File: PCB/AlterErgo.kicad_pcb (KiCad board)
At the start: 2 copper layers, 92 parts, among them J1 GS3, J2 SJ-43514, J3 GS3, SW0:10 SW_Push, SW0:11 SW_Push, SW0:12 SW_Push, SW0:7 SW_Push, SW0:8 SW_Push, SW0:9 SW_Push, SW1 SW_SPST, SW1:10 SW_Push, SW1:11 SW_Push, SW1:12 SW_Push, SW1:13 SW_Push, SW1:9 SW_Push, SW2:10 SW_Push, SW2:11 SW_Push, SW2:12 SW_Push, SW2:13 SW_Push, SW2:7 SW_Push, SW2:8 SW_Push, SW2:9 SW_Push, SW3:10 SW_Push, SW3:11 SW_Push, SW3:12 SW_Push, SW3:13 SW_Push, SW3:8 SW_Push, SW3:9 SW_Push, SW4:10 SW_Push, SW4:11 SW_Push, SW4:12 SW_Push, SW4:13 SW_Push, SW4:7 SW_Push, SW4:8 SW_Push, SW4:9 SW_Push, SW5:10 SW_Push, SW5:11 SW_Push, SW5:12 SW_Push, SW5:13 SW_Push, SW5:7 SW_Push, SW5:8 SW_Push, SW5:9 SW_Push, U1 Feather32u4Bluefruit, U2 MCP23018

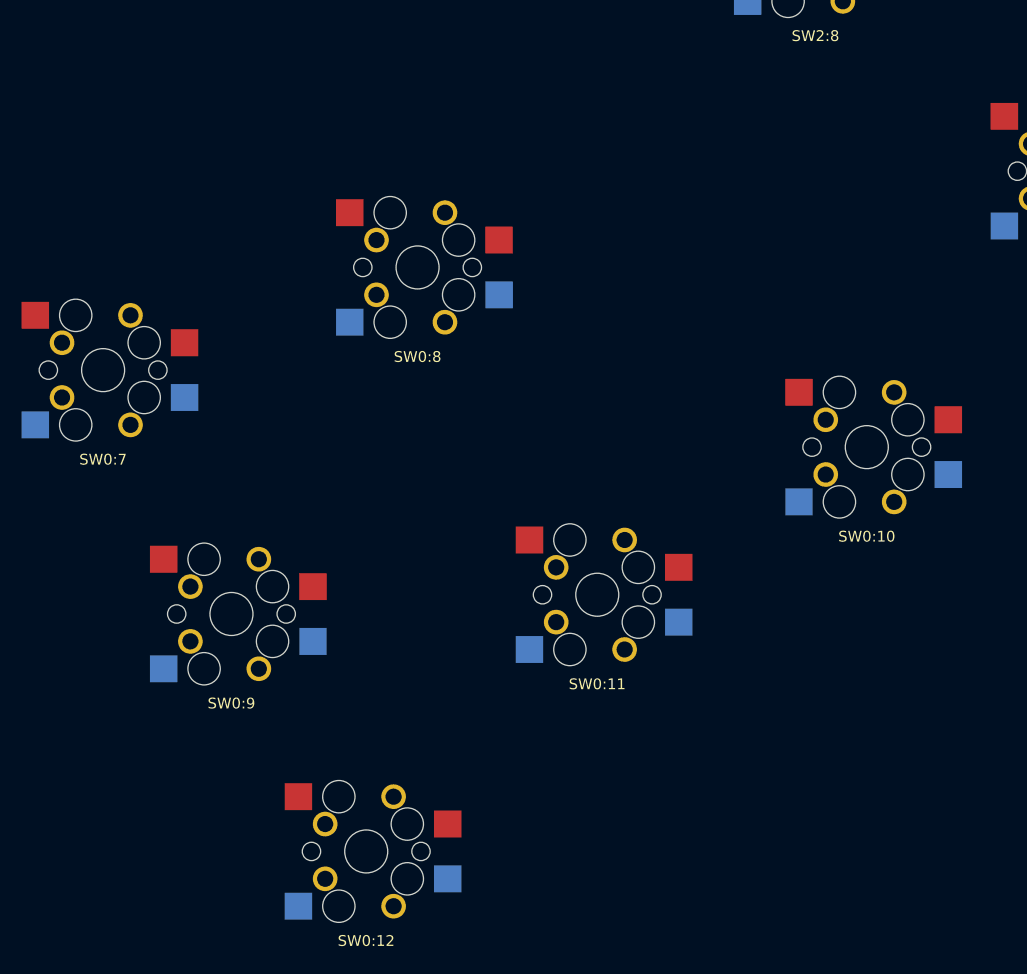
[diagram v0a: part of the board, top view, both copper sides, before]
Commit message: Position thumb cluster switches;
The formulas I used to convert from Keyboard Layout Editor’s U (key units) with center of rotation to absolute coordinates in inches for KiCad can be found in https://www.icloud.com/numbers/0NN-61zf81eeyGf2WznQMhHeA#Key_position_calculations
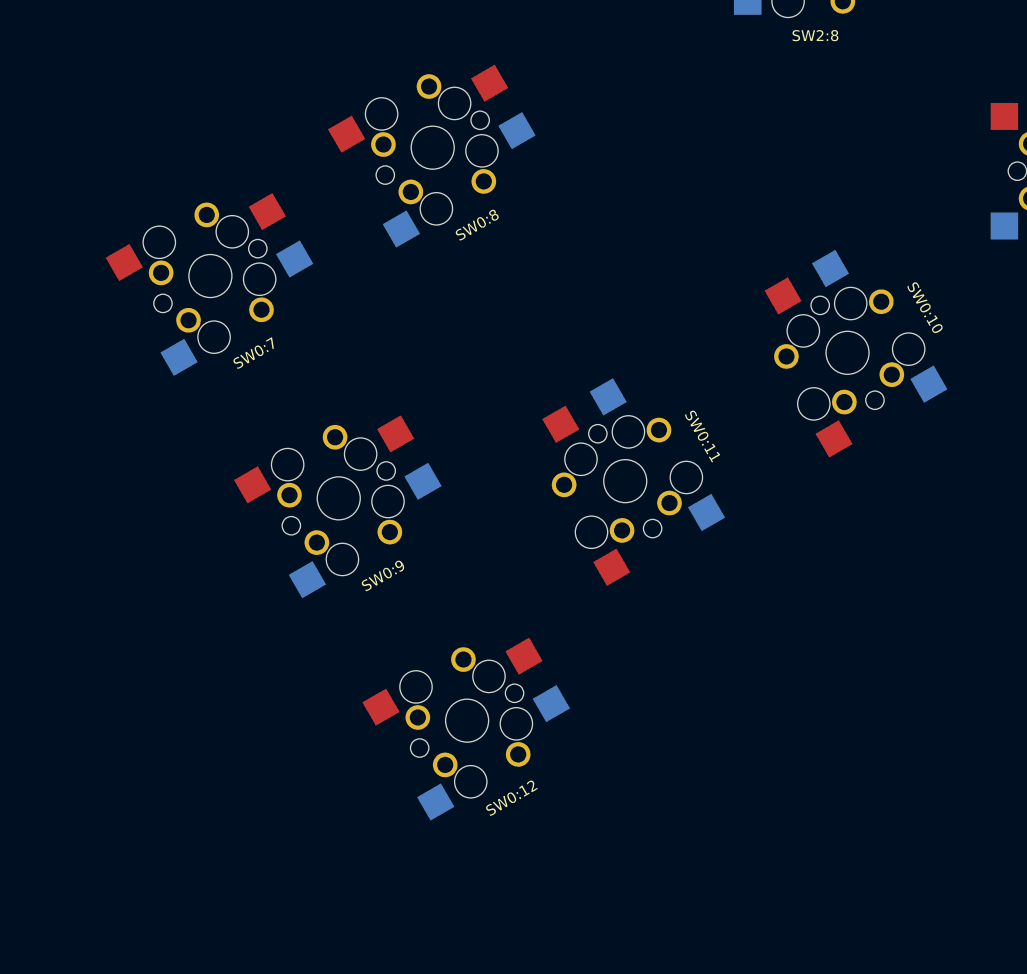
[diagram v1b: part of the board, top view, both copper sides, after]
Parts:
- moved SW0:12 15.3 mm to (74.8, 202.8), turned to 30 degrees
- moved SW0:9 14.6 mm to (62.9, 182.2), turned to 30 degrees
- moved SW0:7 13.2 mm to (51.0, 161.5), turned to 30 degrees
- moved SW0:8 11.2 mm to (71.7, 149.6), turned to 30 degrees
- moved SW0:11 10.9 mm to (89.5, 180.6), turned to 120 degrees
- moved SW0:10 8.93 mm to (110.1, 168.7), turned to 120 degrees

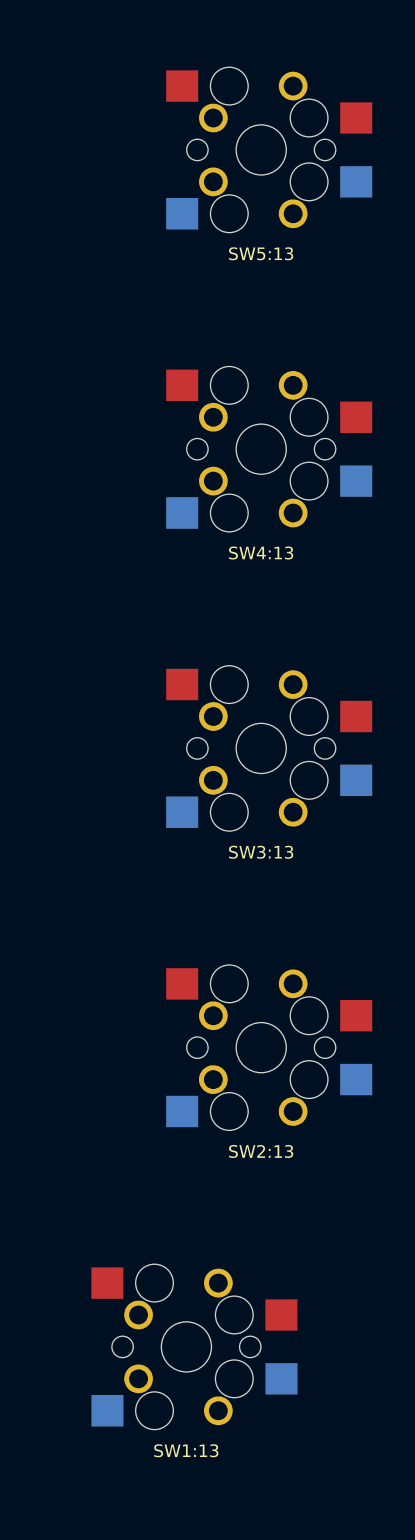
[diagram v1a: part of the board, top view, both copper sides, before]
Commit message: Allow use of 1u or 1.5u keys in all positions on outside column (using the alternate positions will require soldering and will not allow kailh sockets to be used)
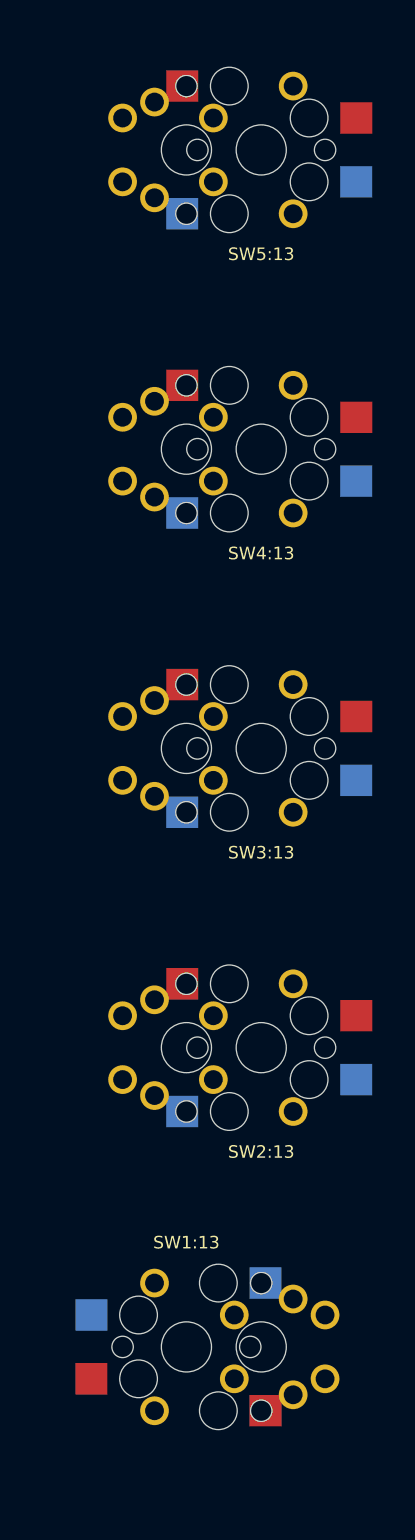
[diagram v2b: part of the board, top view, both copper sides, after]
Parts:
- added ?: MX, keyswitches:MX_reversible, F.Cu at (232.2, 163.7)
- added ?: MX, keyswitches:MX_reversible, F.Cu at (226.2, 68.5)
- added ?: MX, keyswitches:MX_reversible, F.Cu at (226.2, 92.3)
- added ?: MX, keyswitches:MX_reversible, F.Cu at (226.2, 116.1)
- added ?: MX, keyswitches:MX_reversible, F.Cu at (226.2, 139.9)
- turned SW1:13 to 180 degrees

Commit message: Set up design rules
based on https://docs.oshpark.com/design-tools/kicad/kicad-design-rules/
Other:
- net class Default: clearance 0.2 -> 0.1524; trace_width 0.25 -> 0.1524; via_dia 0.6 -> 0.6858; via_drill 0.4 -> 0.3302
- rule pad_to_mask_clearance: 0.2 -> 0.0508
- rule trace_clearance: 0.2 -> 0.1524
- rule trace_min: 0.2 -> 0.1524
- rule via_min_drill: 0.3 -> 0.3302
- rule via_min_size: 0.4 -> 0.6858
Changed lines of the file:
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@@
 (kicad_pcb (version 4) (host pcbnew 4.0.7)
   (general
-    (links 0)
+    (links 388)
     (no_connects 388)
     (area 40.508856 -74.833 449.550001 213.296599)
@@
   )
   (setup
-    (last_trace_width 0.25)
-    (trace_clearance 0.2)
+    (last_trace_width 0.1524)
+    (trace_clearance 0.1524)
     (zone_clearance 0.508)
     (zone_45_only no)
-    (trace_min 0.2)
+    (trace_min 0.1524)
     (segment_width 0.2)
     (edge_width 0.15)
-    (via_size 0.6)
-    (via_drill 0.4)
-    (via_min_size 0.4)
-    (via_min_drill 0.3)
-    (uvia_size 0.3)
-    (uvia_drill 0.1)
+    (via_size 0.6858)
+    (via_drill 0.3302)
+    (via_min_size 0.6858)
+    (via_min_drill 0.3302)
+    (uvia_size 0.6858)
+    (uvia_drill 0.3302)
     (uvias_allowed no)
-    (uvia_min_size 0.2)
-    (uvia_min_drill 0.1)
+    (uvia_min_size 0)
+    (uvia_min_drill 0)
     (pcb_text_width 0.3)
     (pcb_text_size 1.5 1.5)
@@
     (pad_size 2.286 2.286)
     (pad_drill 1.4986)
-    (pad_to_mask_clearance 0.2)
+    (pad_to_mask_clearance 0.0508)
     (aux_axis_origin 0 0)
     (grid_origin 71.4375 47.625)
@@
   (net 82 "Net-(U2-Pad28)")
   (net_class Default "This is the default net class."
-    (clearance 0.2)
-    (trace_width 0.25)
-    (via_dia 0.6)
-    (via_drill 0.4)
-    (uvia_dia 0.3)
-    (uvia_drill 0.1)
+    (clearance 0.1524)
+    (trace_width 0.1524)
+    (via_dia 0.6858)
+    (via_drill 0.3302)
+    (uvia_dia 0.6858)
+    (uvia_drill 0.3302)
     (add_net +3V3)
     (add_net /COL0)
@@
     (add_net "Net-(U2-Pad28)")
   )
+  (module keyswitches:Kailh_socket_optional_reversible (layer F.Cu)
+    (at 107.15628 107.1563)
+    (descr "MX-style keyswitch with support for reversible optional Kailh socket")
+    (tags MX,cherry,gateron,kailh,pg1511,socket)
+    (fp_text reference SW3:8 (at 0 8.3) (layer F.SilkS)
+      (effects (font (size 1 1) (thickness 0.15)))
+    )
+    (fp_text value SW_Push (at 0 -8.7) (layer F.Fab)
+      (effects (font (size 1 1) (thickness 0.15)))
+    )
+    (fp_line (start -7 -6) (end -7 -7) (layer B.SilkS) (width 0.15))
+    (fp_line (start -7 -7) (end -6 -7) (layer B.SilkS) (width 0.15))
+    (fp_line (start -6 7) (end -7 7) (layer B.SilkS) (width 0.15))
+    (fp_line (start -7 7) (end -7 6) (layer B.SilkS) (width 0.15))
+    (fp_line (start 7 6) (end 7 7) (layer B.SilkS) (width 0.15))
+    (fp_line (start 7 7) (end 6 7) (layer B.SilkS) (width 0.15))
+    (fp_line (start 6 -7) (end 7 -7) (layer B.SilkS) (width 0.15))
+    (fp_line (start 7 -7) (end 7 -6) (layer B.SilkS) (width 0.15))
+    (fp_line (start -6.9 6.9) (end 6.9 6.9) (layer Eco2.User) (width 0.15))
+    (fp_line (start 6.9 -6.9) (end -6.9 -6.9) (layer Eco2.User) (width 0.15))
+    (fp_line (start 6.9 -6.9) (end 6.9 6.9) (layer Eco2.User) (width 0.15))
+    (fp_line (start -6.9 6.9) (end -6.9 -6.9) (layer Eco2.User) (width 0.15))
+    (fp_line (start -7.5 -7.5) (end 7.5 -7.5) (layer Eco2.User) (width 0.15))
+    (fp_line (start 7.5 -7.5) (end 7.5 7.5) (layer Eco2.User) (width 0.15))
+    (fp_line (start 7.5 7.5) (end -7.5 7.5) (layer Eco2.User) (width 0.15))
+    (fp_line (start -7.5 7.5) (end -7.5 -7.5) (layer Eco2.User) (width 0.15))
+    (pad 1 smd rect (at -6.29 5.08) (size 2.55 2.5) (layers B.Cu B.Paste B.Mask)
+      (net 64 /ROW3))
+    (pad 2 smd rect (at 7.56 2.54) (size 2.55 2.5) (layers B.Cu B.Paste B.Mask)
+      (net 32 "Net-(D3:8-Pad2)"))
+    (pad "" np_thru_hole circle (at -2.54 -5.08) (size 3 3) (drill 3) (layers *.Cu *.Mask))
+    (pad "" np_thru_hole circle (at 3.81 -2.54) (size 3 3) (drill 3) (layers *.Cu *.Mask))
+    (pad 2 thru_hole circle (at 2.54 5.08) (size 2.286 2.286) (drill 1.4986) (layers *.Cu *.Mask)
+      (net 32 "Net-(D3:8-Pad2)"))
+    (pad 1 thru_hole circle (at -3.81 2.54) (size 2.286 2.286) (drill 1.4986) (layers *.Cu *.Mask)
+      (net 64 /ROW3))
+    (pad 1 smd rect (at -6.29 -5.08) (size 2.55 2.5) (layers F.Cu F.Paste F.Mask)
+      (net 64 /ROW3))
+    (pad "" np_thru_hole circle (at -2.54 5.08) (size 3 3) (drill 3) (layers *.Cu *.Mask))
+    (pad "" np_thru_hole circle (at 3.81 2.54) (size 3 3) (drill 3) (layers *.Cu *.Mask))
+    (pad 2 thru_hole circle (at 2.54 -5.08) (size 2.286 2.286) (drill 1.4986) (layers *.Cu *.Mask)
+      (net 32 "Net-(D3:8-Pad2)"))
+    (pad "" np_thru_hole circle (at 0 0) (size 3.9878 3.9878) (drill 3.9878) (layers *.Cu *.Mask))
+    (pad 1 thru_hole circle (at -3.81 -2.54) (size 2.286 2.286) (drill 1.4986) (layers *.Cu *.Mask)
+      (net 64 /ROW3))
+    (pad "" np_thru_hole circle (at 5.08 0) (size 1.7018 1.7018) (drill 1.7018) (layers *.Cu *.Mask))
+    (pad "" np_thru_hole circle (at -5.08 0) (size 1.7018 1.7018) (drill 1.7018) (layers *.Cu *.Mask))
+    (pad 2 smd rect (at 7.56 -2.54) (size 2.55 2.5) (layers F.Cu F.Paste F.Mask)
+      (net 32 "Net-(D3:8-Pad2)"))
+  )
   (module keyswitches:MX_reversible (layer F.Cu)
     (at 232.17201 163.711035 270)
@@
   )
   (module keyswitches:Kailh_socket_optional_reversible (layer F.Cu)
-    (at 107.15628 107.1563)
-    (descr "MX-style keyswitch with support for reversible optional Kailh socket")
-    (tags MX,cherry,gateron,kailh,pg1511,socket)
-    (fp_text reference SW3:8 (at 0 8.3) (layer F.SilkS)
-      (effects (font (size 1 1) (thickness 0.15)))
-    )
-    (fp_text value SW_Push (at 0 -8.7) (layer F.Fab)
-      (effects (font (size 1 1) (thickness 0.15)))
-    )
-    (fp_line (start -7 -6) (end -7 -7) (layer B.SilkS) (width 0.15))
-    (fp_line (start -7 -7) (end -6 -7) (layer B.SilkS) (width 0.15))
-    (fp_line (start -6 7) (end -7 7) (layer B.SilkS) (width 0.15))
-    (fp_line (start -7 7) (end -7 6) (layer B.SilkS) (width 0.15))
-    (fp_line (start 7 6) (end 7 7) (layer B.SilkS) (width 0.15))
-    (fp_line (start 7 7) (end 6 7) (layer B.SilkS) (width 0.15))
-    (fp_line (start 6 -7) (end 7 -7) (layer B.SilkS) (width 0.15))
-    (fp_line (start 7 -7) (end 7 -6) (layer B.SilkS) (width 0.15))
-    (fp_line (start -6.9 6.9) (end 6.9 6.9) (layer Eco2.User) (width 0.15))
-    (fp_line (start 6.9 -6.9) (end -6.9 -6.9) (layer Eco2.User) (width 0.15))
-    (fp_line (start 6.9 -6.9) (end 6.9 6.9) (layer Eco2.User) (width 0.15))
-    (fp_line (start -6.9 6.9) (end -6.9 -6.9) (layer Eco2.User) (width 0.15))
-    (fp_line (start -7.5 -7.5) (end 7.5 -7.5) (layer Eco2.User) (width 0.15))
-    (fp_line (start 7.5 -7.5) (end 7.5 7.5) (layer Eco2.User) (width 0.15))
-    (fp_line (start 7.5 7.5) (end -7.5 7.5) (layer Eco2.User) (width 0.15))
-    (fp_line (start -7.5 7.5) (end -7.5 -7.5) (layer Eco2.User) (width 0.15))
-    (pad 1 smd rect (at -6.29 5.08) (size 2.55 2.5) (layers B.Cu B.Paste B.Mask)
-      (net 64 /ROW3))
-    (pad 2 smd rect (at 7.56 2.54) (size 2.55 2.5) (layers B.Cu B.Paste B.Mask)
-      (net 32 "Net-(D3:8-Pad2)"))
-    (pad "" np_thru_hole circle (at -2.54 -5.08) (size 3 3) (drill 3) (layers *.Cu *.Mask))
-    (pad "" np_thru_hole circle (at 3.81 -2.54) (size 3 3) (drill 3) (layers *.Cu *.Mask))
-    (pad 2 thru_hole circle (at 2.54 5.08) (size 2.286 2.286) (drill 1.4986) (layers *.Cu *.Mask)
-      (net 32 "Net-(D3:8-Pad2)"))
-    (pad 1 thru_hole circle (at -3.81 2.54) (size 2.286 2.286) (drill 1.4986) (layers *.Cu *.Mask)
-      (net 64 /ROW3))
-    (pad 1 smd rect (at -6.29 -5.08) (size 2.55 2.5) (layers F.Cu F.Paste F.Mask)
-      (net 64 /ROW3))
-    (pad "" np_thru_hole circle (at -2.54 5.08) (size 3 3) (drill 3) (layers *.Cu *.Mask))
-    (pad "" np_thru_hole circle (at 3.81 2.54) (size 3 3) (drill 3) (layers *.Cu *.Mask))
-    (pad 2 thru_hole circle (at 2.54 -5.08) (size 2.286 2.286) (drill 1.4986) (layers *.Cu *.Mask)
-      (net 32 "Net-(D3:8-Pad2)"))
-    (pad "" np_thru_hole circle (at 0 0) (size 3.9878 3.9878) (drill 3.9878) (layers *.Cu *.Mask))
-    (pad 1 thru_hole circle (at -3.81 -2.54) (size 2.286 2.286) (drill 1.4986) (layers *.Cu *.Mask)
-      (net 64 /ROW3))
-    (pad "" np_thru_hole circle (at 5.08 0) (size 1.7018 1.7018) (drill 1.7018) (layers *.Cu *.Mask))
-    (pad "" np_thru_hole circle (at -5.08 0) (size 1.7018 1.7018) (drill 1.7018) (layers *.Cu *.Mask))
-    (pad 2 smd rect (at 7.56 -2.54) (size 2.55 2.5) (layers F.Cu F.Paste F.Mask)
-      (net 32 "Net-(D3:8-Pad2)"))
-  )
-  (module keyswitches:Kailh_socket_optional_reversible (layer F.Cu)
